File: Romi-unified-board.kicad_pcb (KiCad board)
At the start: 4 copper layers, 125.1 x 125.8 mm, 73 parts, among them J1 ServoAnalog, J10 LIDAR_DATA, J11 LIDAR_MOTOR, J12 ROMI-Encoder, J13 ROMI-Encoder, J14 THING, J15 THING, J16 Conn_01x03_Male, J17 Conn_01x03_Male, J18 Conn_01x03_Male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

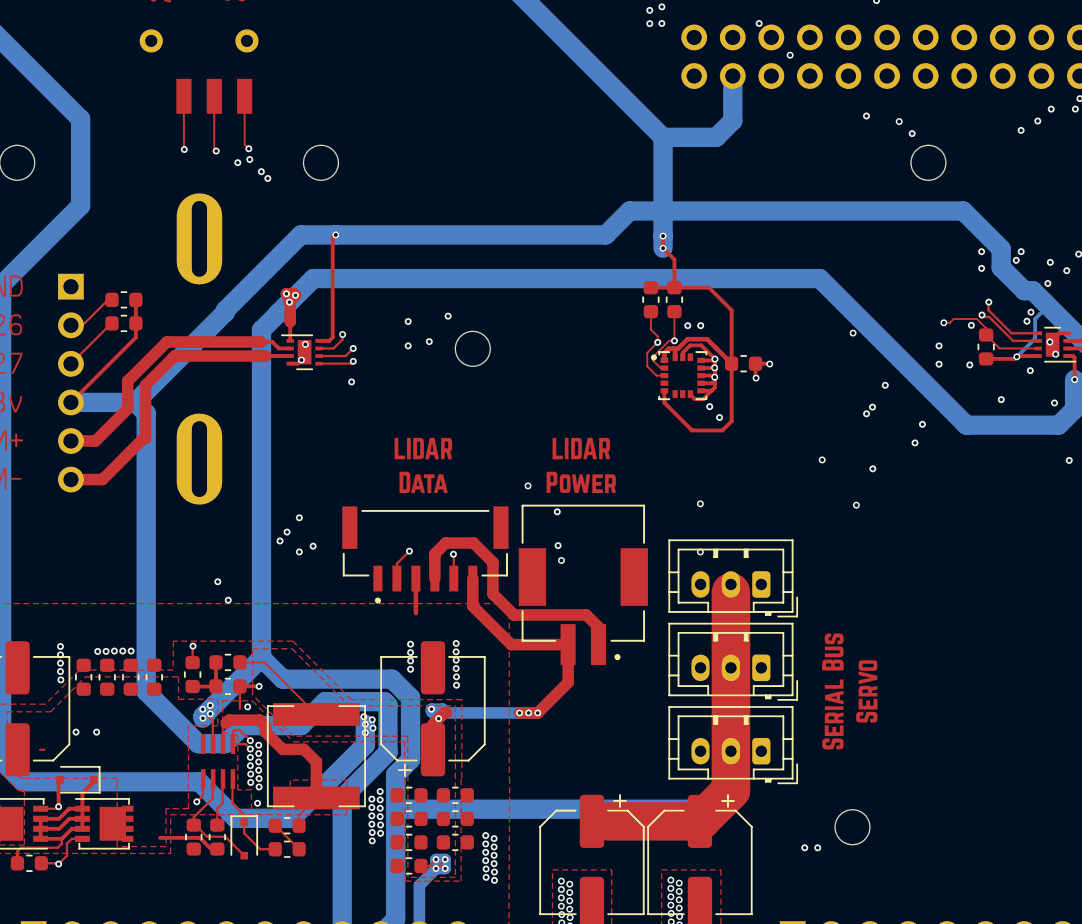
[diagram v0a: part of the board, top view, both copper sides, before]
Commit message: added fiducials
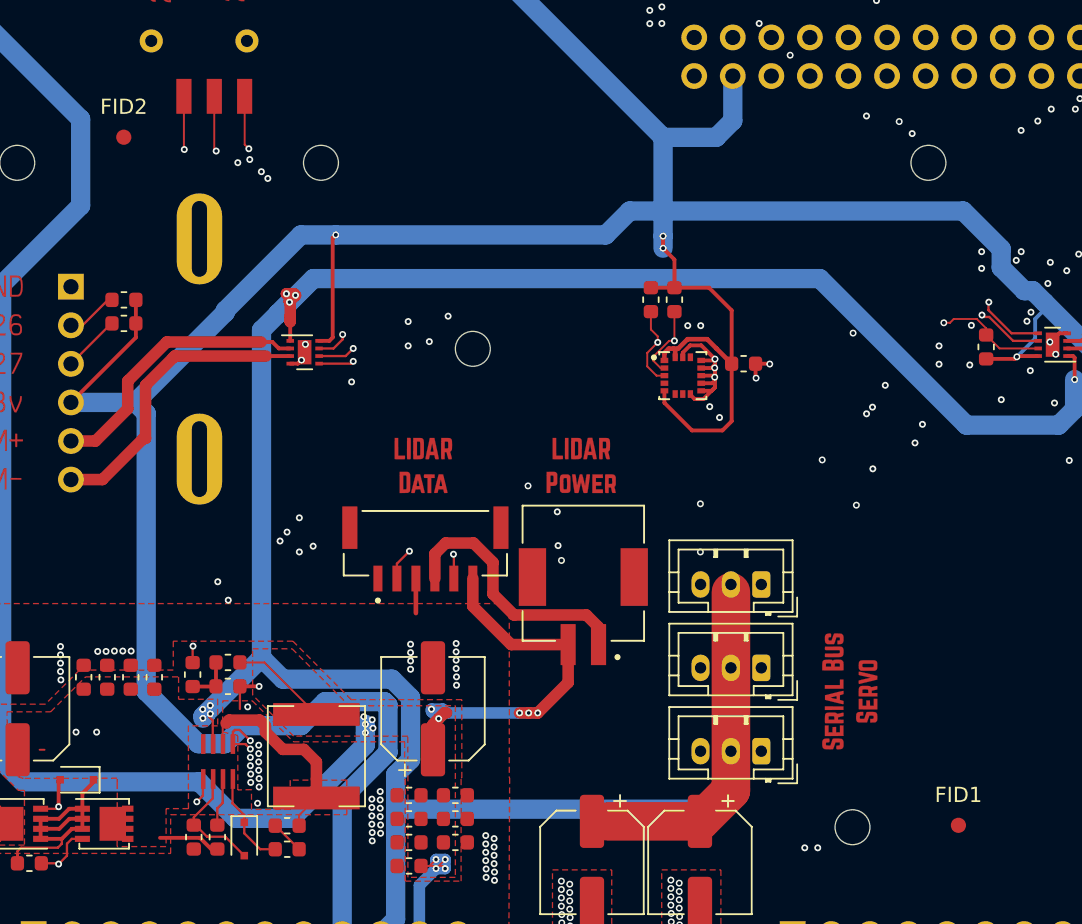
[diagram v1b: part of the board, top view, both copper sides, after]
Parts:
- added FID1: Fiducial, Fiducial:Fiducial_1mm_Mask2mm, F.Cu at (140.9, 139.9)
- added FID2: Fiducial, Fiducial:Fiducial_1mm_Mask2mm, F.Cu at (85.9, 94.6)

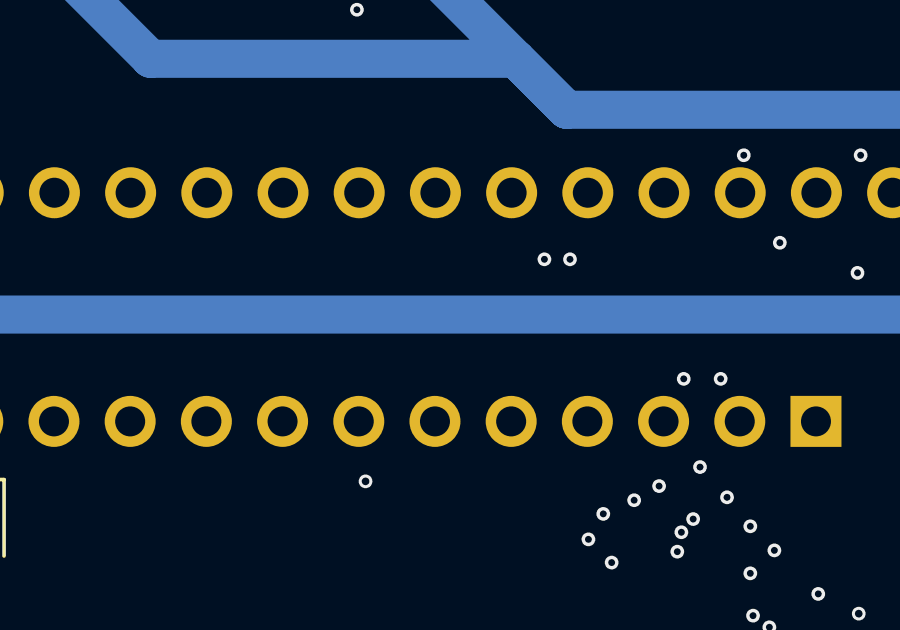
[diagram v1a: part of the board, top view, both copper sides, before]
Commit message: Fixed error in netlist.
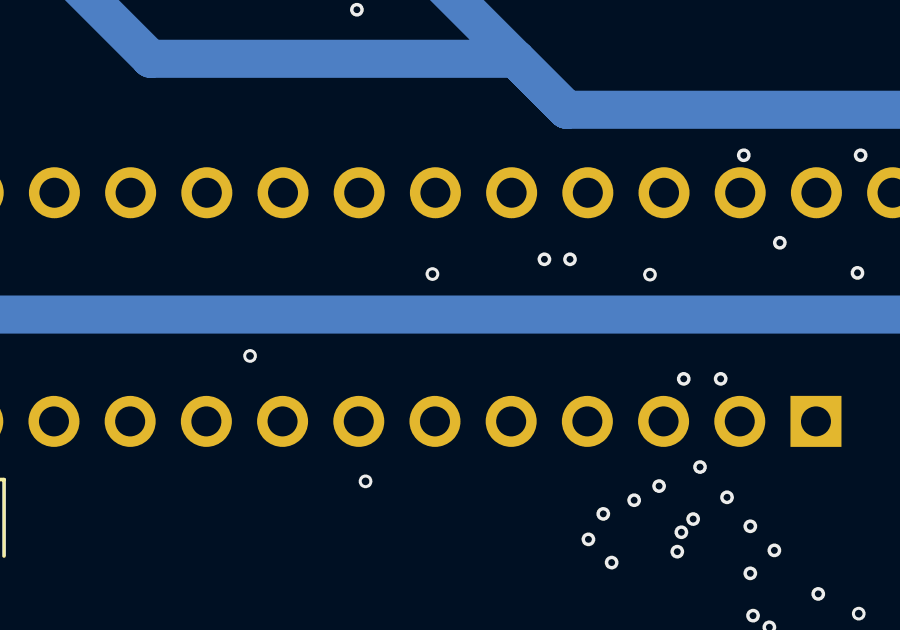
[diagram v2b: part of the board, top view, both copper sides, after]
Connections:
- J2 pad 11: Net-(J2-Pad11) -> GPIO27
- J2 pad 12: Net-(J2-Pad12) -> GPIO14
- J2 pad 13: Net-(J2-Pad13) -> GPIO12
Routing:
- net GPIO14: track 102.1 -> 127.8 mm, vias 4 -> 6
- net GPIO12: track 114.5 -> 124.2 mm, vias 8 -> 9
- net GPIO27: track 175.0 -> 183.7 mm

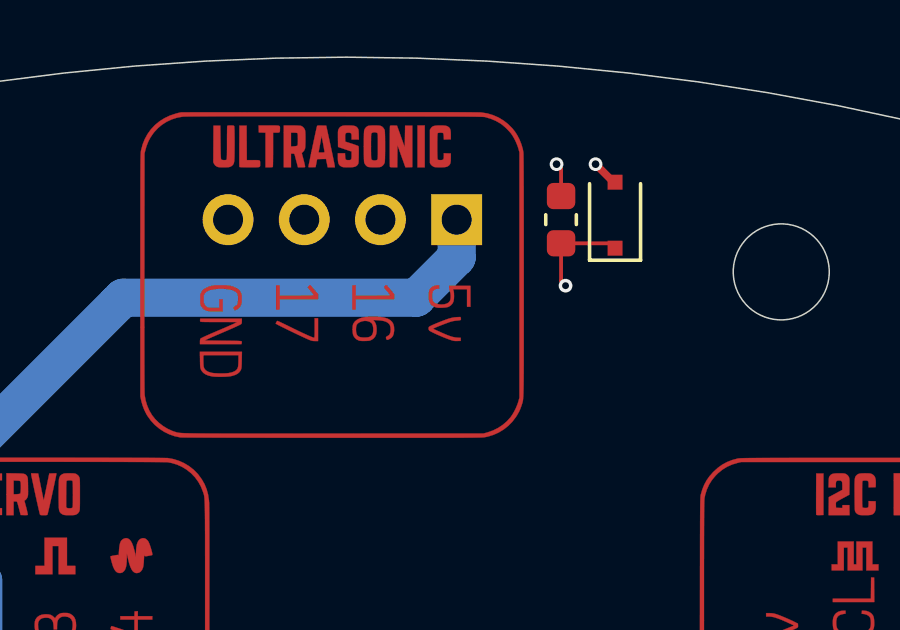
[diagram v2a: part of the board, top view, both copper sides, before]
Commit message: Swapped pins 16 and 17
#10
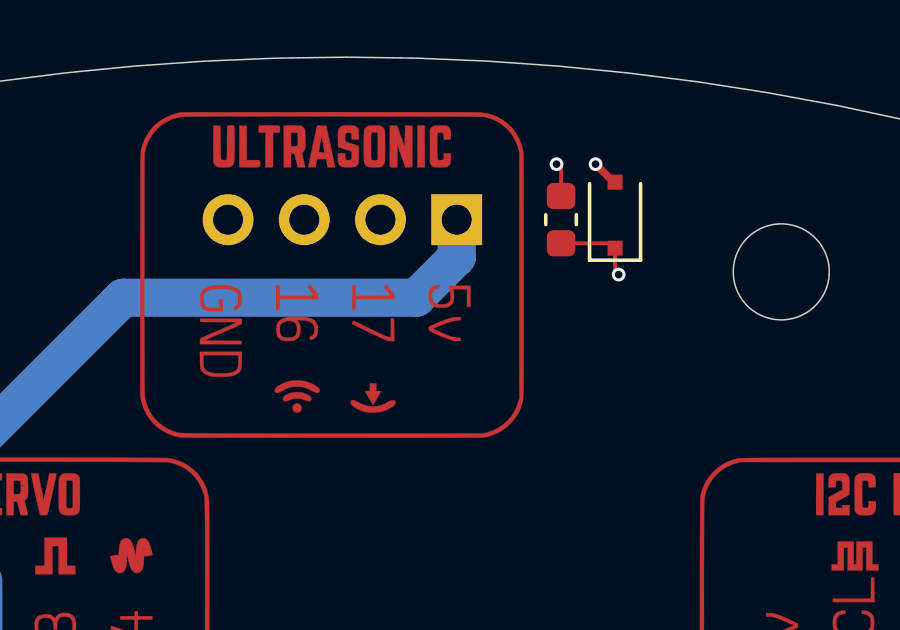
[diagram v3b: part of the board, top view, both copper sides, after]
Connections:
- D1 pad 1: GPIO16 -> GPIO17
- J7 pad 3: GPIO17 -> GPIO16
- R1 pad 1: GPIO16 -> GPIO17
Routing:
- net GPIO17: track 195.1 -> 180.4 mm, vias 9 -> 10
- net GPIO16: track 161.8 -> 168.1 mm, vias 9 -> 8
- net GPIO15: track 249.4 -> 250.4 mm

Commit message: Trace edit.
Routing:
- net GPIO15: track 250.4 -> 251.7 mm
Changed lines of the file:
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@@
     (thickness 1.6)
     (drawings 52)
-    (tracks 1829)
+    (tracks 1831)
     (zones 0)
     (modules 75)
@@
   (segment (start 151.354 74.514) (end 151.354 70.2615) (width 0.127) (layer In1.Cu) (net 27) (status 20))
   (segment (start 155.11 78.27) (end 151.354 74.514) (width 0.127) (layer In1.Cu) (net 27))
-  (segment (start 99.608704 39.108704) (end 97.11 36.61) (width 0.762) (layer In2.Cu) (net 27) (status 20))
-  (segment (start 100.738704 39.108704) (end 99.608704 39.108704) (width 0.762) (layer In2.Cu) (net 27))
-  (segment (start 110.101296 39.108704) (end 100.738704 39.108704) (width 0.127) (layer In2.Cu) (net 27))
   (segment (start 117.43 31.78) (end 110.101296 39.108704) (width 0.127) (layer In2.Cu) (net 27))
   (segment (start 167.93581 54.463486) (end 162.112324 48.64) (width 0.127) (layer In2.Cu) (net 27))
@@
   (segment (start 134.3 33.79) (end 132.68 33.79) (width 0.127) (layer In2.Cu) (net 27))
   (segment (start 132.68 33.79) (end 130.67 31.78) (width 0.127) (layer In2.Cu) (net 27))
+  (segment (start 108.358704 39.108704) (end 107.491296 39.108704) (width 0.127) (layer In2.Cu) (net 27))
+  (segment (start 110.101296 39.108704) (end 108.358704 39.108704) (width 0.127) (layer In2.Cu) (net 27))
+  (segment (start 107.491296 39.108704) (end 105.92 40.68) (width 0.127) (layer In2.Cu) (net 27))
+  (segment (start 101.18 40.68) (end 97.11 36.61) (width 0.127) (layer In2.Cu) (net 27))
+  (segment (start 105.92 40.68) (end 101.18 40.68) (width 0.127) (layer In2.Cu) (net 27))
   (segment (start 98.4087 121.5204) (end 99.3699 122.4816) (width 0.127) (layer In2.Cu) (net 28))
   (segment (start 99.3699 122.4816) (end 111.4725 122.4816) (width 0.127) (layer In2.Cu) (net 28))

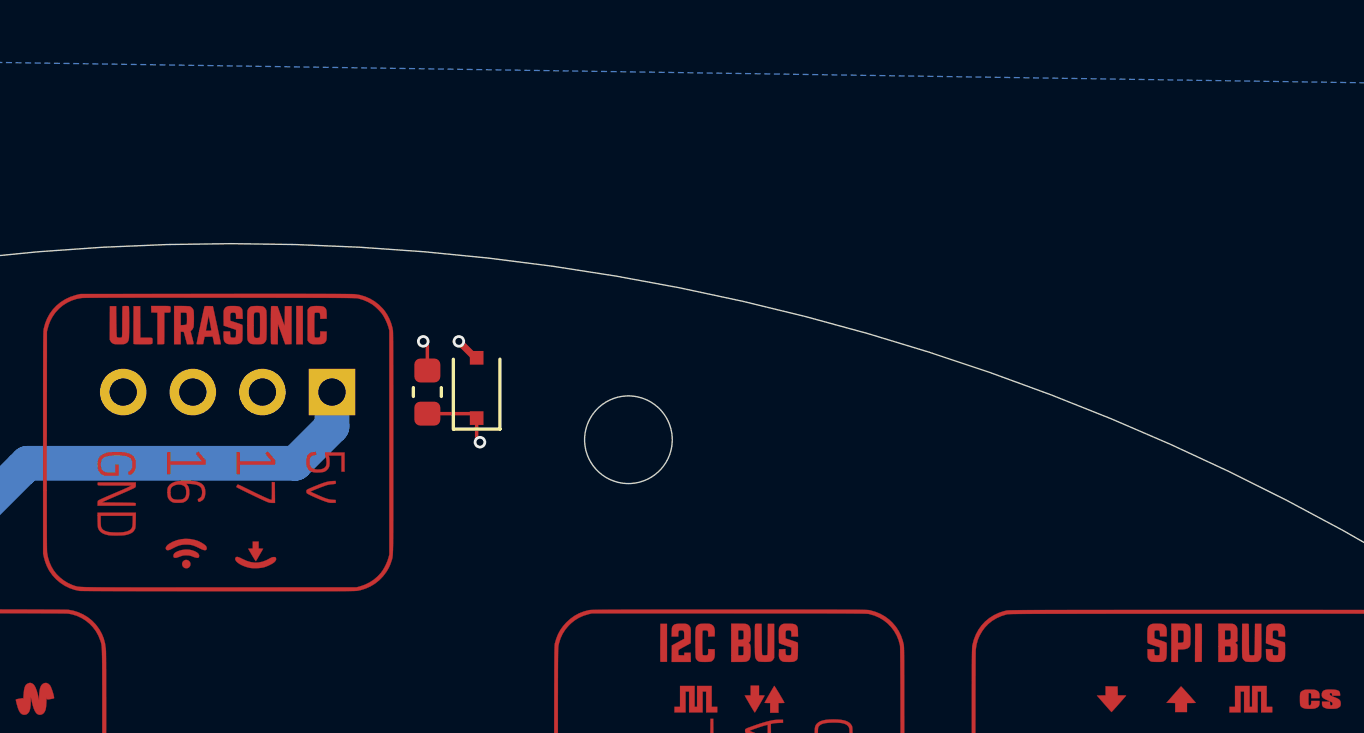
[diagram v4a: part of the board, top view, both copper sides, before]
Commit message: Fixed  ultrasonic
#10
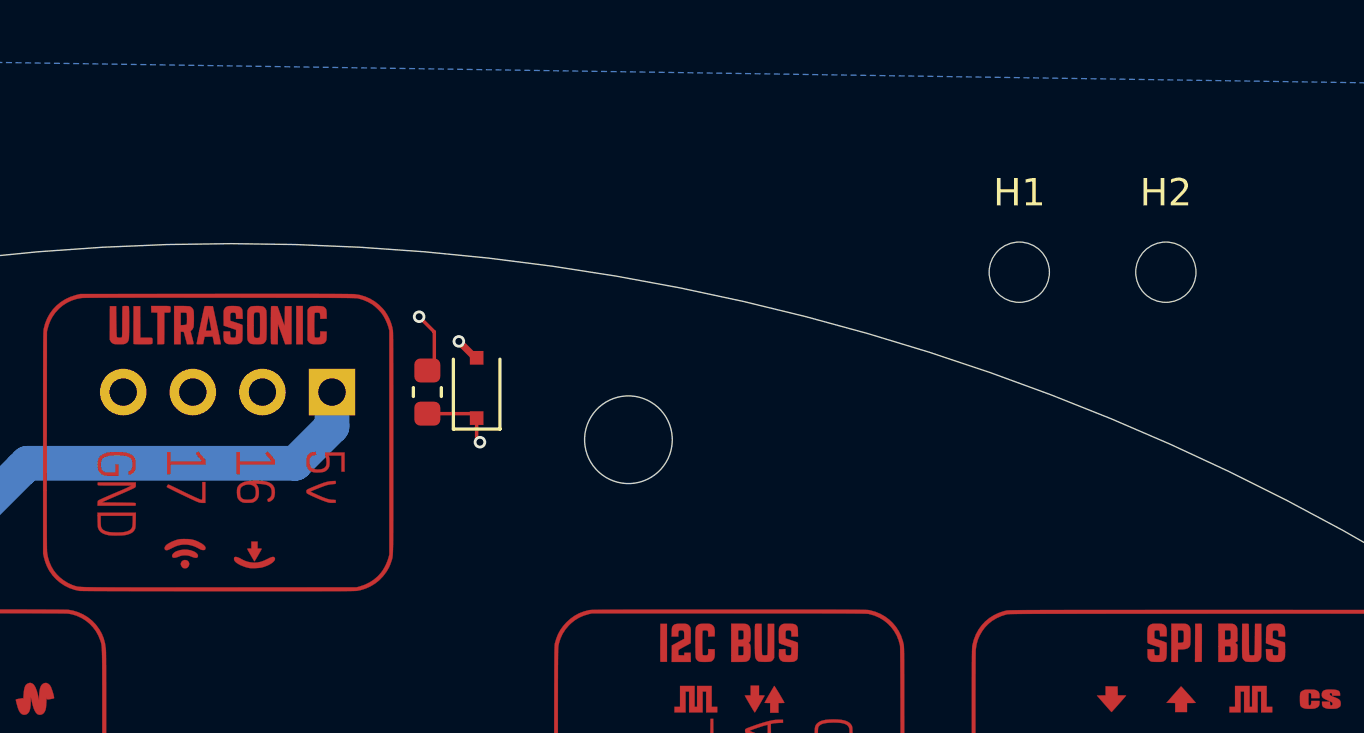
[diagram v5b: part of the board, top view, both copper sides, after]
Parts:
- added H1: MountingHole, MountingHole:MountingHole_2.2mm_M2_DIN965, F.Cu at (147.9, 31.2)
- added H2: MountingHole, MountingHole:MountingHole_2.2mm_M2_DIN965, F.Cu at (153.2, 31.2)
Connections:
- J7 pad 2: Net-(J7-Pad2) -> GPIO16
- J7 pad 3: GPIO16 -> Net-(J7-Pad3)
- R1 pad 2: Net-(J7-Pad2) -> Net-(J7-Pad3)
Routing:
- net Net-(J7-Pad3): track 0.00 -> 11.7 mm, vias 0 -> 1
- net Net-(J7-Pad2): track 7.78 -> 0.00 mm, vias 1 -> 0
- net GPIO16: track 168.1 -> 167.2 mm
